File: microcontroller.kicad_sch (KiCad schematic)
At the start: 52 parts, among them J100 Conn_01x05_Pin, J101 Conn_01x03, J102 TC2030, J103 Screw_Terminal_01x02, J104 USB_C_Receptacle_USB2.0_16P, SW100 SW_Push, U100 STM32H563RITx, U101 AP2112K-3.3, U102 USBLC6-2SC6, Y100 16MHz

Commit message: Footprints added
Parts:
- C100, C107, C109, C112, C113, C114, C115, C117: footprint (none) -> Capacitor_SMD:C_0201_0603Metric
- C101, C102, C103, C104, C105, C106, C108, C110, C111, C116, D106, F100, FB100: footprint (none) -> Capacitor_SMD:C_01005_0402Metric
- D100, D101, D102, D103, D104: footprint (none) -> Diode_SMD:D_SOD-323
- J100: footprint (none) -> Connector_PinHeader_2.54mm:PinHeader_1x05_P2.54mm_Vertical
- J101: footprint (none) -> Connector_PinHeader_2.54mm:PinHeader_1x03_P2.54mm_Vertical
- J103: footprint (none) -> TerminalBlock_Phoenix:TerminalBlock_Phoenix_MPT-0,5-2-2.54_1x02_P2.54mm_Horizontal
- L100: footprint (none) -> Inductor_SMD:L_0201_0603Metric
- R100, R101, R102, R103, R104, R105, R106, R107, R108, R109: footprint (none) -> Resistor_SMD:R_01005_0402Metric
- SW100: footprint (none) -> Button_Switch_SMD:SW_SPST_B3S-1000
- TP100, TP101, TP102, TP103: footprint (none) -> TestPoint:TestPoint_Pad_D2.0mm
- Y100: footprint (none) -> Crystal:Crystal_SMD_EuroQuartz_MJ-4Pin_5.0x3.2mm

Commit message: Some changes to power circuitry, more layout
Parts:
- C100, C107, C109, C112, C113, C114, C115, C117: footprint Capacitor_SMD:C_0201_0603Metric -> Capacitor_SMD:C_0603_1608Metric
- C101, C102, C103, C104, C105, C106, C108, C110, C111, C116: footprint Capacitor_SMD:C_01005_0402Metric -> Capacitor_SMD:C_0402_1005Metric
- D106: footprint Capacitor_SMD:C_01005_0402Metric -> LED_SMD:LED_0402_1005Metric
- F100, FB100: footprint Capacitor_SMD:C_01005_0402Metric -> Capacitor_SMD:C_0603_1608Metric
- L100: footprint Inductor_SMD:L_0201_0603Metric -> Inductor_SMD:L_0603_1608Metric
- R100, R101, R102, R103, R104, R105, R106, R107, R108, R109: footprint Resistor_SMD:R_01005_0402Metric -> Resistor_SMD:R_0402_1005Metric
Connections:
- net +5V: now also C115.1, L100.2; no longer D105.1 (K), F100.2
- net +VDC: now also F100.1; no longer C113.1, L100.1
- new net: C113.1, D105.1 (K), F100.2, L100.1
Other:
- moved on the sheet: C113, C115, D105, F100, L100, TP101

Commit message: Extremely incomplete, preliminary, pre-alpha, ugly layout
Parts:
- C107, C109: footprint Capacitor_SMD:C_0603_1608Metric -> Capacitor_SMD:C_0402_1005Metric
- TP102: footprint TestPoint:TestPoint_Pad_D2.0mm -> TestPoint:TestPoint_Pad_D1.0mm
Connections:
- net +3.3V is gone; now on net +3V3: C100.1, C103.1, C104.1, C106.1, C108.1, C110.1, C111.1, J101.3 (Pin_3), R100.1, U100.1 (VBAT), U100.13 (VDDA), U100.19 (VDD), U100.32 (VDD), U100.48 (VDD), U100.64 (VDD)

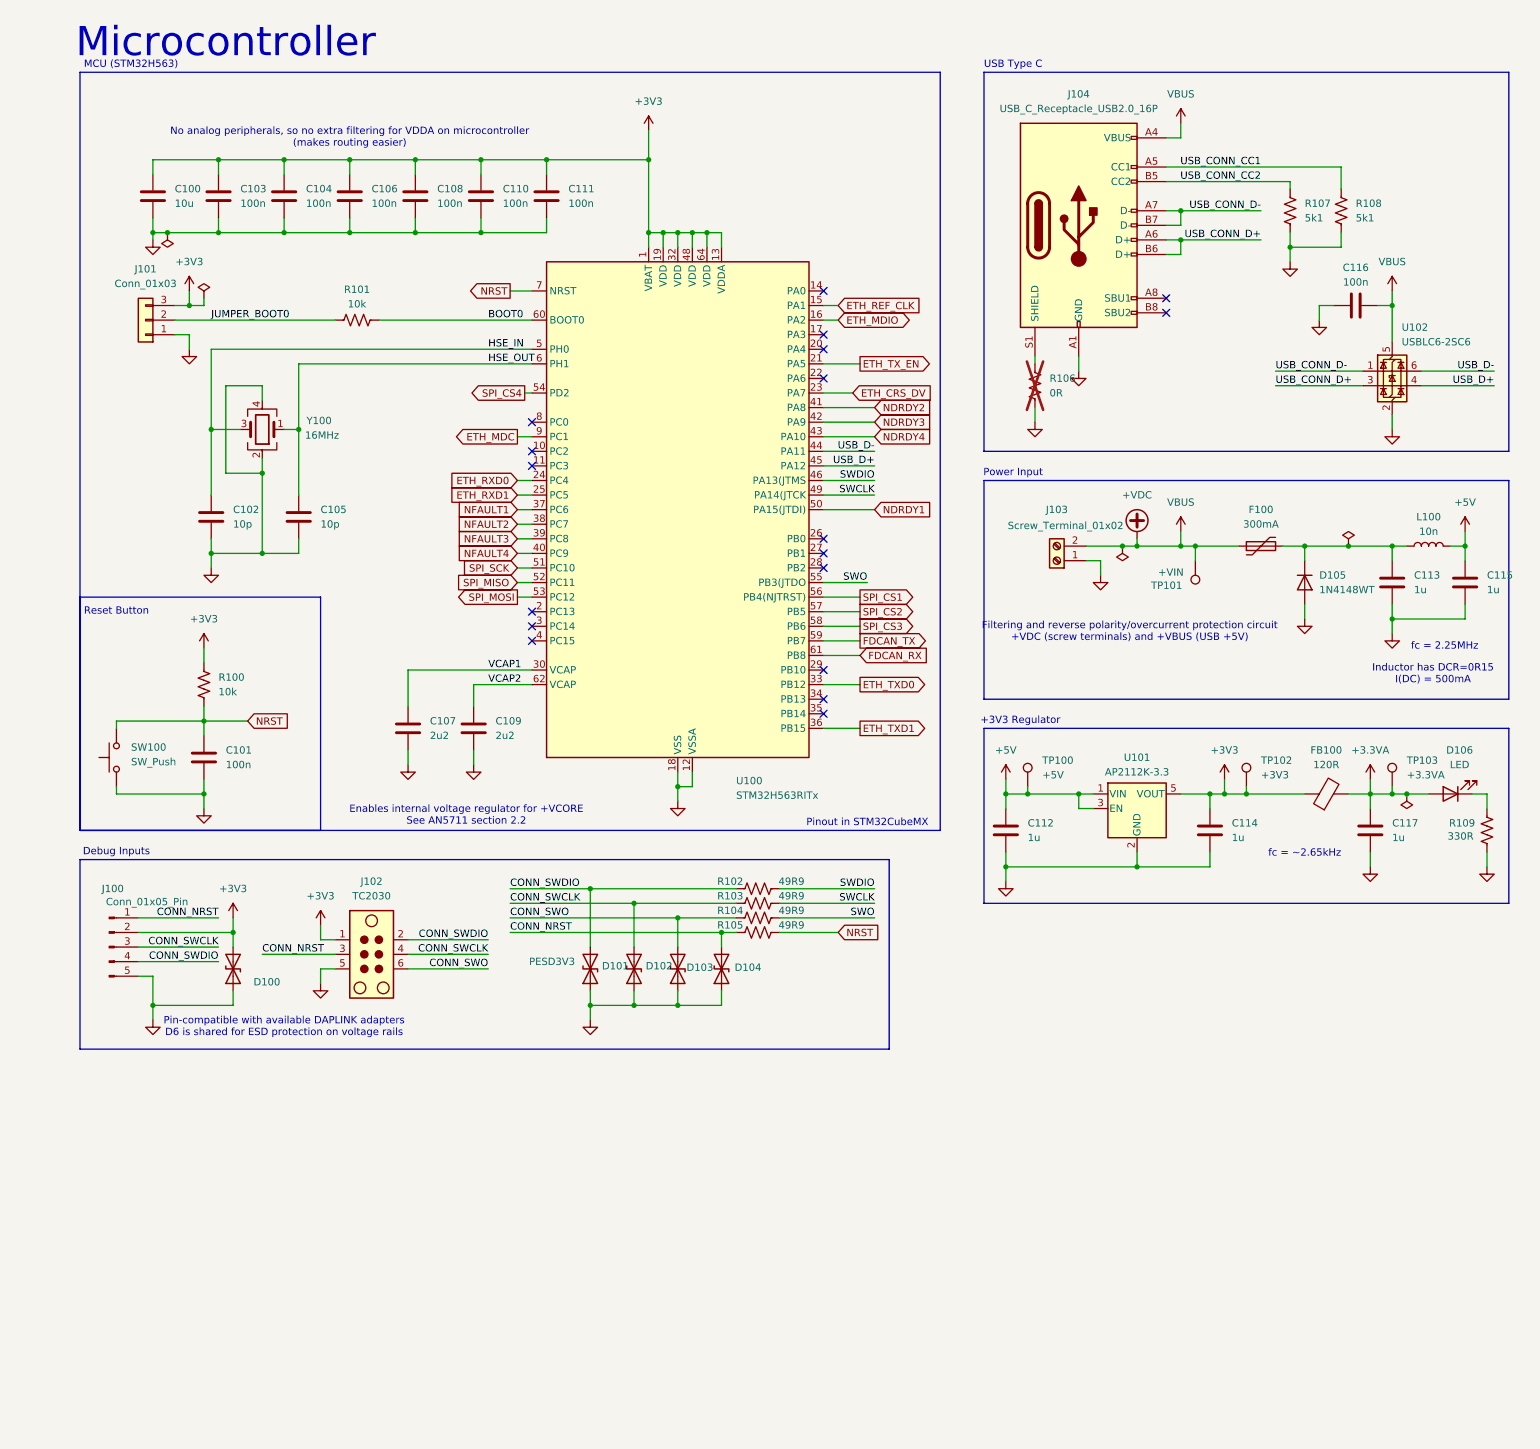
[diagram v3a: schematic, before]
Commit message: First decent layout
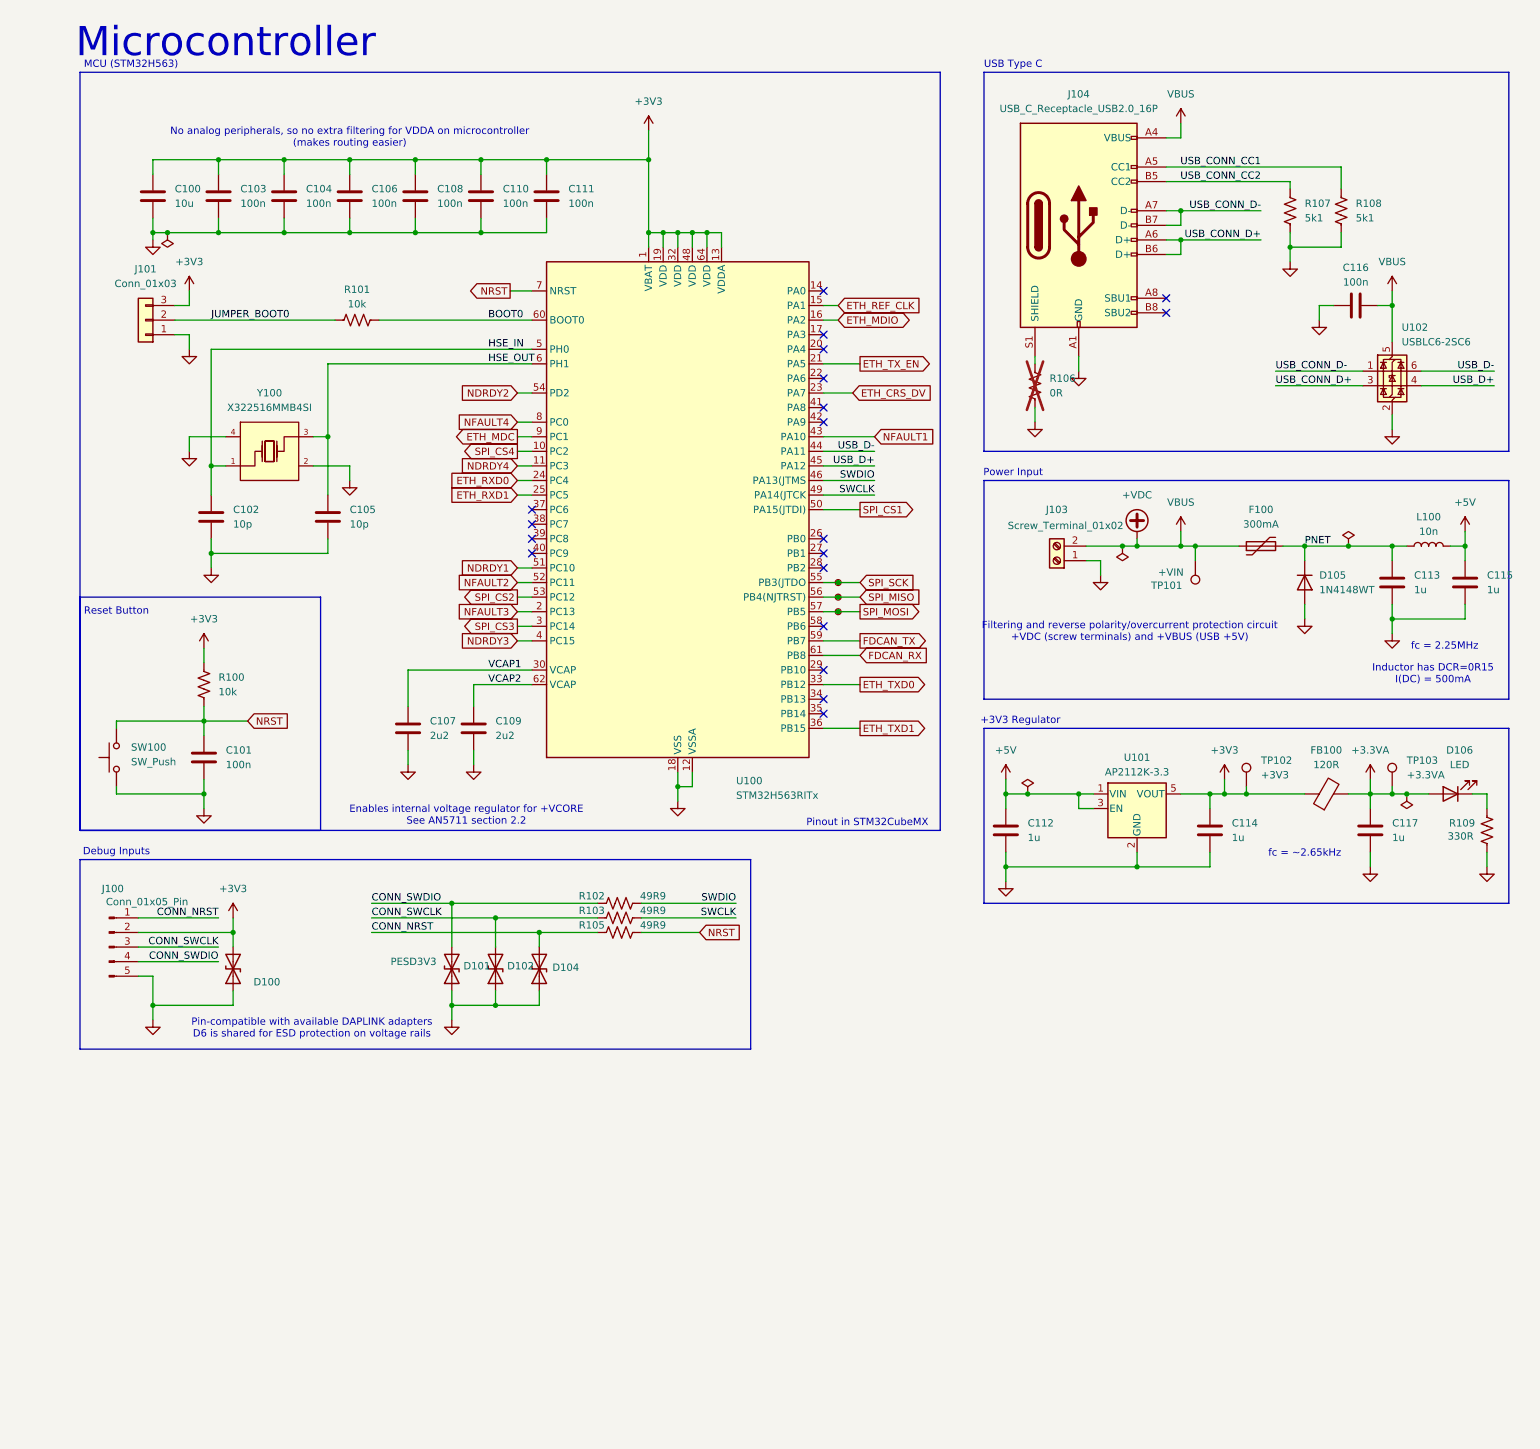
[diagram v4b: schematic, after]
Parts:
- removed D103: PESD3V3, Diode_SMD:D_SOD-323, symbol Device:D_TVS
- removed J102: TC2030, Connector:Tag-Connect_TC2030-IDC-NL_2x03_P1.27mm_Vertical, symbol Connector:TC2030
- removed R104: 49R9, Resistor_SMD:R_0402_1005Metric, symbol Device:R_US
- removed TP100: +5V, TestPoint:TestPoint_Pad_D2.0mm, symbol Connector:TestPoint
- removed Y100: 16MHz, Crystal:Crystal_SMD_EuroQuartz_MJ-4Pin_5.0x3.2mm, symbol Device:Crystal_GND24
- added TP100, TP104, TP105: TestPoint_Small, TestPoint:TestPoint_Pad_D1.0mm, symbol Connector:TestPoint_Small
- added Y100: X322516MMB4SI, Library:CRYSTAL-SMD_4P-L2.0-W1.6-BL, symbol lcsc:X322516MMB4SI
- J104: footprint Connector_USB:USB_C_Receptacle_HRO_TYPE-C-31-M-12 -> Library:USB_C_Receptacle_HRO_TYPE-C-31-M-12
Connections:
- net SWO is gone; now on net SPI_SCK: U100.55 (PB3(JTDO)
- net GND: now also Y100.2, Y100.4
- net HSE_IN: now also Y100.1
- net HSE_OUT: now also Y100.3
- net NDRDY1: now also U100.51 (PC10); no longer U100.50 (PA15(JTDI))
- net NDRDY2: now also U100.54 (PD2); no longer U100.41 (PA8)
- net NDRDY3: now also U100.4 (PC15); no longer U100.42 (PA9)
- net NDRDY4: now also U100.11 (PC3); no longer U100.43 (PA10)
- net NFAULT1: now also U100.43 (PA10); no longer U100.37 (PC6)
- net NFAULT2: now also U100.52 (PC11); no longer U100.38 (PC7)
- net NFAULT3: now also U100.2 (PC13); no longer U100.39 (PC8)
- net NFAULT4: now also U100.8 (PC0); no longer U100.40 (PC9)
- net SPI_CS1: now also U100.50 (PA15(JTDI)); no longer U100.56 (PB4(NJTRST))
- net SPI_CS2: now also U100.53 (PC12); no longer U100.57 (PB5)
- net SPI_CS3: now also U100.3 (PC14); no longer U100.58 (PB6)
- net SPI_CS4: now also U100.10 (PC2); no longer U100.54 (PD2)
- net SPI_MISO: now also U100.56 (PB4(NJTRST)), TP104.1; no longer U100.52 (PC11)
- net SPI_MOSI: now also U100.57 (PB5), TP105.1; no longer U100.53 (PC12)
- net SPI_SCK: now also TP100.1; no longer U100.51 (PC10)
- net PNET: now reaches C113.1, D105.1 (K), F100.2, L100.1
- no-connect marks 18 -> 19
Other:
- moved on the sheet: C105, D101, D102, D104, R102, R103, R105

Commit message: Post-stitch
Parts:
- added TP111: +5V, TestPoint:TestPoint_Pad_D1.5mm, symbol Connector:TestPoint
- TP101: footprint TestPoint:TestPoint_Pad_D2.0mm -> TestPoint:TestPoint_Pad_D1.5mm
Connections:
- net PNET: now also TP111.1

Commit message: I hate everything
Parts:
- removed TP101: +VIN, TestPoint:TestPoint_Pad_D1.5mm, symbol Connector:TestPoint
- removed TP102: +3V3, TestPoint:TestPoint_Pad_D1.0mm, symbol Connector:TestPoint
- removed TP111: +5V, TestPoint:TestPoint_Pad_D1.5mm, symbol Connector:TestPoint
- added C118, C119, C120, C121, C122, C123: 22u, Capacitor_SMD:C_0805_2012Metric, symbol Device:C
- added D103, D107, D108, D109: LED, LED_SMD:LED_0402_1005Metric, symbol Device:LED
- added F101: 500mA, Capacitor_SMD:C_0603_1608Metric, symbol Device:Polyfuse
- added JP100: Jumper_2_Bridged, Connector_PinHeader_2.54mm:PinHeader_1x02_P2.54mm_Vertical, symbol Jumper:Jumper_2_Bridged
- added R104, R110, R111, R112: 330R, Resistor_SMD:R_0402_1005Metric, symbol Device:R_US
- added TP101, TP102, TP111: TestPoint_Small, TestPoint:TestPoint_Pad_D1.0mm, symbol Connector:TestPoint_Small
- SW100: footprint Button_Switch_SMD:SW_SPST_B3S-1000 -> Button_Switch_SMD:SW_Push_1P1T_NO_CK_KSC6xxG
- TP103: footprint TestPoint:TestPoint_Pad_D2.0mm -> TestPoint:TestPoint_Pad_D1.5mm
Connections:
- net +3V3: now also C121.2, C122.2, C123.2, TP102.1
- net +5V: now also C118.2, C119.2, C120.2
- net +VDC: now also J103.1 (Pin_1), D103.2 (A), JP100.1 (A), TP101.1; no longer C116.2, J103.2 (Pin_2), J104.A4 (VBUS), J104.A9 (VBUS), J104.B4 (VBUS), J104.B9 (VBUS), U102.5 (VBUS)
- net GND: now also J103.2 (Pin_2), C118.1, C119.1, C120.1, C121.1, C122.1, C123.1, R104.2, R110.1, R111.1, R112.1; no longer J103.1 (Pin_1)
- net PNET: now also TP111.1
- net USER_LED_1: now reaches U100.38 (PC7)
- net USER_LED_1: now also D107.2 (A)
- net USER_LED_2: now reaches U100.39 (PC8)
- net USER_LED_2: now also D108.2 (A)
- net USER_LED_3: now reaches U100.40 (PC9)
- net USER_LED_3: now also D109.2 (A)
- net STDBY: now reaches U100.41 (PA8)
- new net: F101.1, JP100.2 (B)
- new net: D108.1 (K), R111.2
- new net: D103.1 (K), R104.1
- new net: D109.1 (K), R112.2
- new net: D107.1 (K), R110.2
- new net VBUS: C116.2, F101.2, J104.A4 (VBUS), J104.A9 (VBUS), J104.B4 (VBUS), J104.B9 (VBUS), U102.5 (VBUS)
- no-connect marks 19 -> 15
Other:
- note added: "USB Power Bridge"
- moved on the sheet: C114, D101, D102, D104, J103, R102, R103, R105

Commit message: First workable layout
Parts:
- removed D105: 1N4148WT, Diode_SMD:D_SOD-523, symbol Diode:1N4148WT
- removed SW100: SW_Push, Button_Switch_SMD:SW_Push_1P1T_NO_CK_KSC6xxG, symbol Switch:SW_Push
- added D105: MRA4007T3G, Diode_SMD:D_SMA, symbol Diode:MRA4007T3G
- added SW100: K2-1157SP-I4SW-04, Library:SW-SMD_4P-L6.2-W6.2-P4.50-LS8.6, symbol lcsc:K2-1157SP-I4SW-04
- added TP112: TestPoint_Small, TestPoint:TestPoint_Pad_D1.0mm, symbol Connector:TestPoint_Small
- C100: LCSC (none) -> C19702
- C101, C103, C104, C106, C108, C110, C111, C116: LCSC (none) -> C1525
- C102, C105: LCSC (none) -> C32949
- C107, C109: LCSC (none) -> C170151
- C112, C113, C114, C115, C117: LCSC (none) -> C15849
- C118, C119, C120, C121, C122, C123: LCSC (none) -> C602037
- D100, D101, D102, D104: LCSC (none) -> C51450
- D103, D106, D107, D108, D109: LCSC (none) -> C965793
- F100: LCSC (none) -> C19193027
- F101: LCSC (none) -> C883095
- FB100: LCSC (none) -> C41330
- J100, J101, JP100: LCSC (none) -> C2337
- J103: LCSC (none) -> C3029316
- J104: LCSC (none) -> C165948
- L100: LCSC (none) -> C1589
- R100, R101: LCSC (none) -> C60490
- R102, R103, R105: LCSC (none) -> C87044
- R104, R109, R110, R111, R112: LCSC (none) -> C105875
- R106: LCSC (none) -> C106231
- R107, R108: LCSC (none) -> C105873
- U100: LCSC (none) -> C20619634
- U101: LCSC (none) -> C51118
- U102: LCSC (none) -> C7519
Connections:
- net GND: now also D105.2 (A), SW100.3, SW100.4, TP112.1
- net NRST: now also SW100.1, SW100.2
- net PNET: now also D105.1 (K)
- net USB_FUSE: now reaches F101.1, JP100.2 (B)
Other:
- note added: "Bulk Caps"
- note removed: "USB Power Bridge"
- moved on the sheet: C118, C119, C120, C121, C122, C123, D100, D101, D102, D104, F101, R102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
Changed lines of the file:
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@@
 	(title_block
 		(title "Thermocouple Board")
-		(date "2025-10-07")
+		(date "2025-10-09")
 		(rev "1A")
 		(company "Aggie Propulsion and Rocketry Lab")

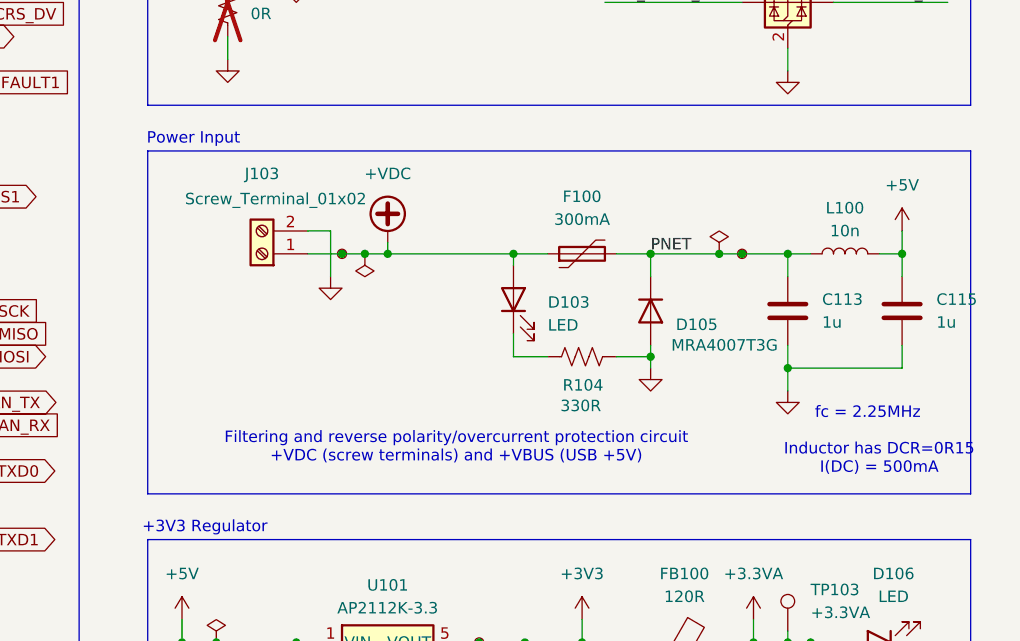
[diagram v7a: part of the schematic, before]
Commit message: Added pfet for reverse polarity protection, moved power circuitry away from analog parts
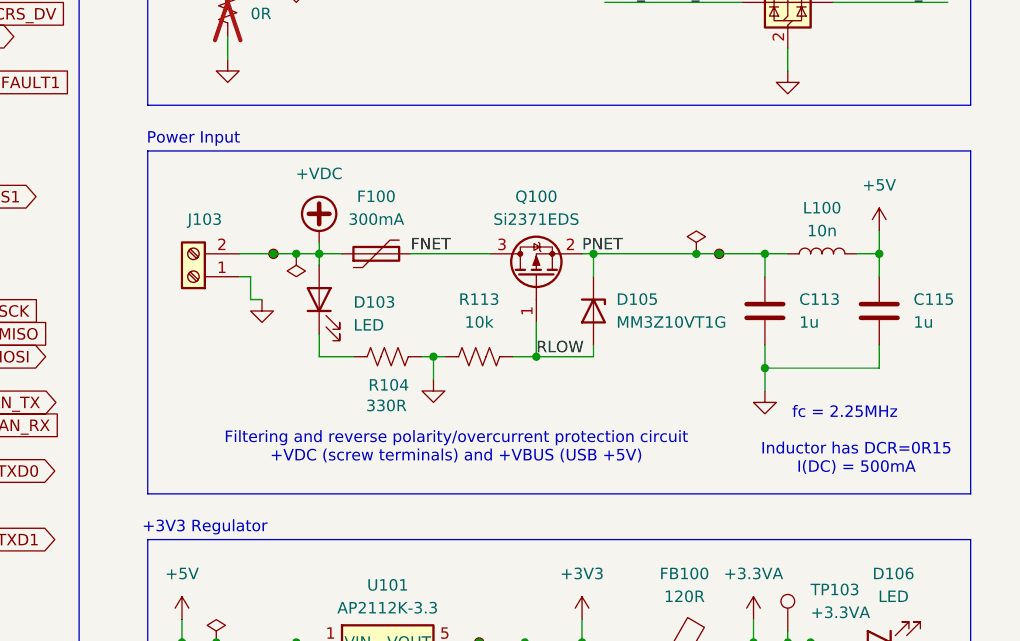
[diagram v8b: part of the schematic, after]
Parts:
- removed D105: MRA4007T3G, Diode_SMD:D_SMA, symbol Diode:MRA4007T3G
- added D105: MM3Z10VT1G, Diode_SMD:D_SOD-323, symbol Diode:BZX384xxxx
- added Q100: Si2371EDS, Package_TO_SOT_SMD:SOT-23, symbol Transistor_FET:Si2371EDS
- added R113: 10k, Resistor_SMD:R_0402_1005Metric, symbol Device:R_US
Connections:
- net +VDC: now also J103.2 (Pin_2); no longer J103.1 (Pin_1)
- net GND: now also J103.1 (Pin_1), R113.1; no longer J103.2 (Pin_2)
- net PNET: now also D105.1 (K), Q100.2 (S); no longer F100.2
- new net FNET: F100.2, Q100.3 (D)
- new net RLOW: D105.2 (A), Q100.1 (G), R113.2
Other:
- moved on the sheet: C113, C115, D103, F100, J103, L100, R104
